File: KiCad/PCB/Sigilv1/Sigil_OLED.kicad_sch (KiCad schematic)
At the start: 3 parts, among them J2 INLAND 1.3" OLED HEADER (7-PI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, J3 BUZZER LOGICAL ONLY, U1 REMOVABLE ESP32 DEVKIT / 2 x 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

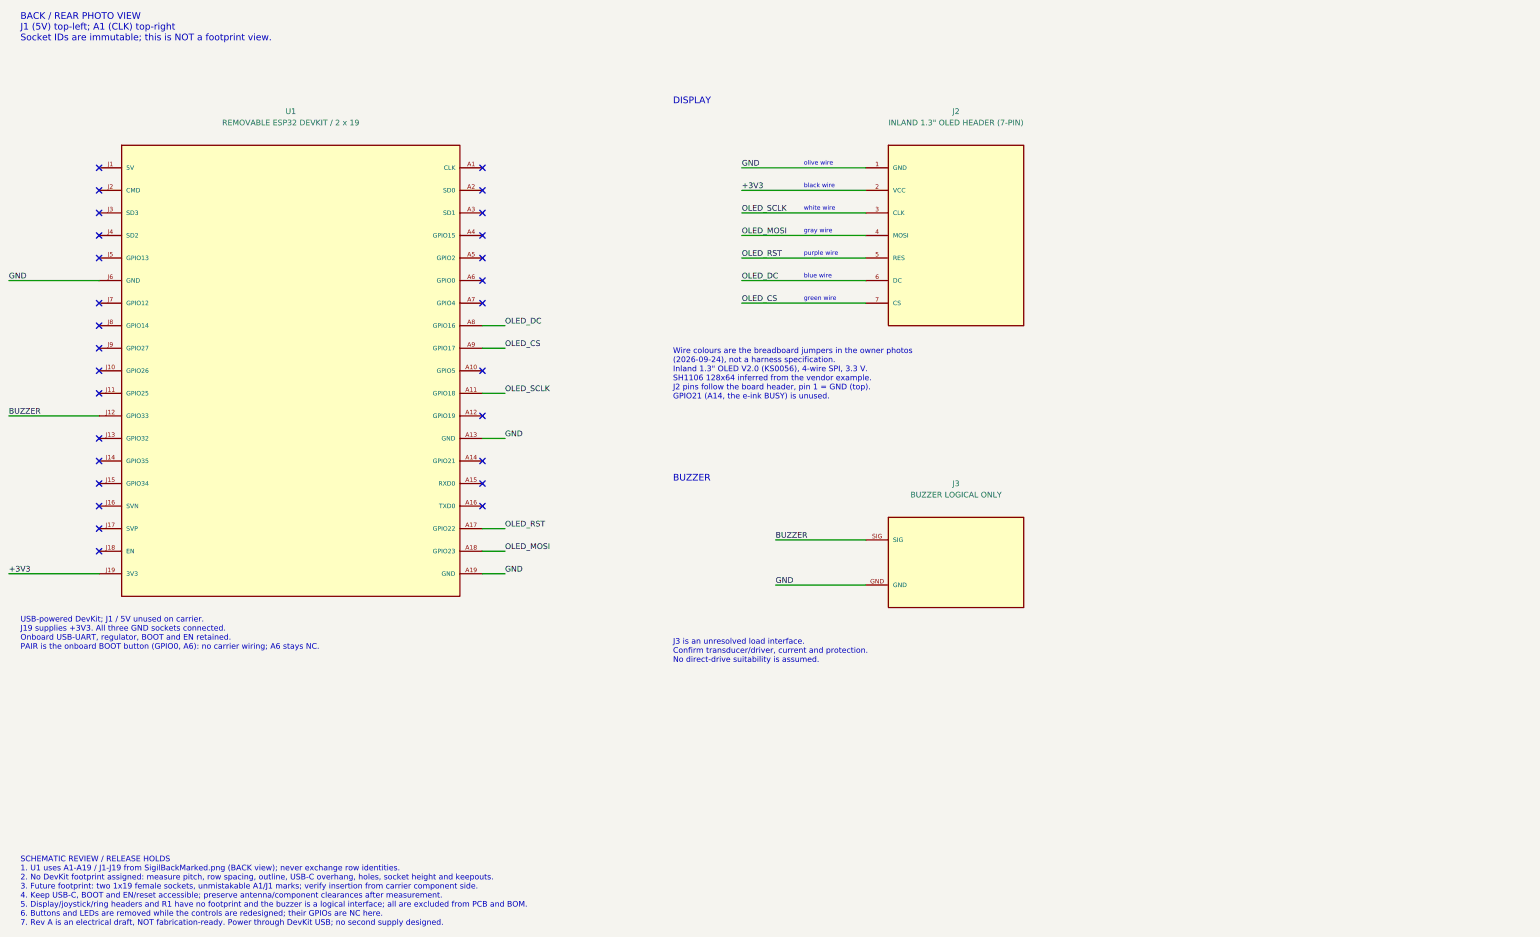
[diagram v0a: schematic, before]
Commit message: New LED Ring
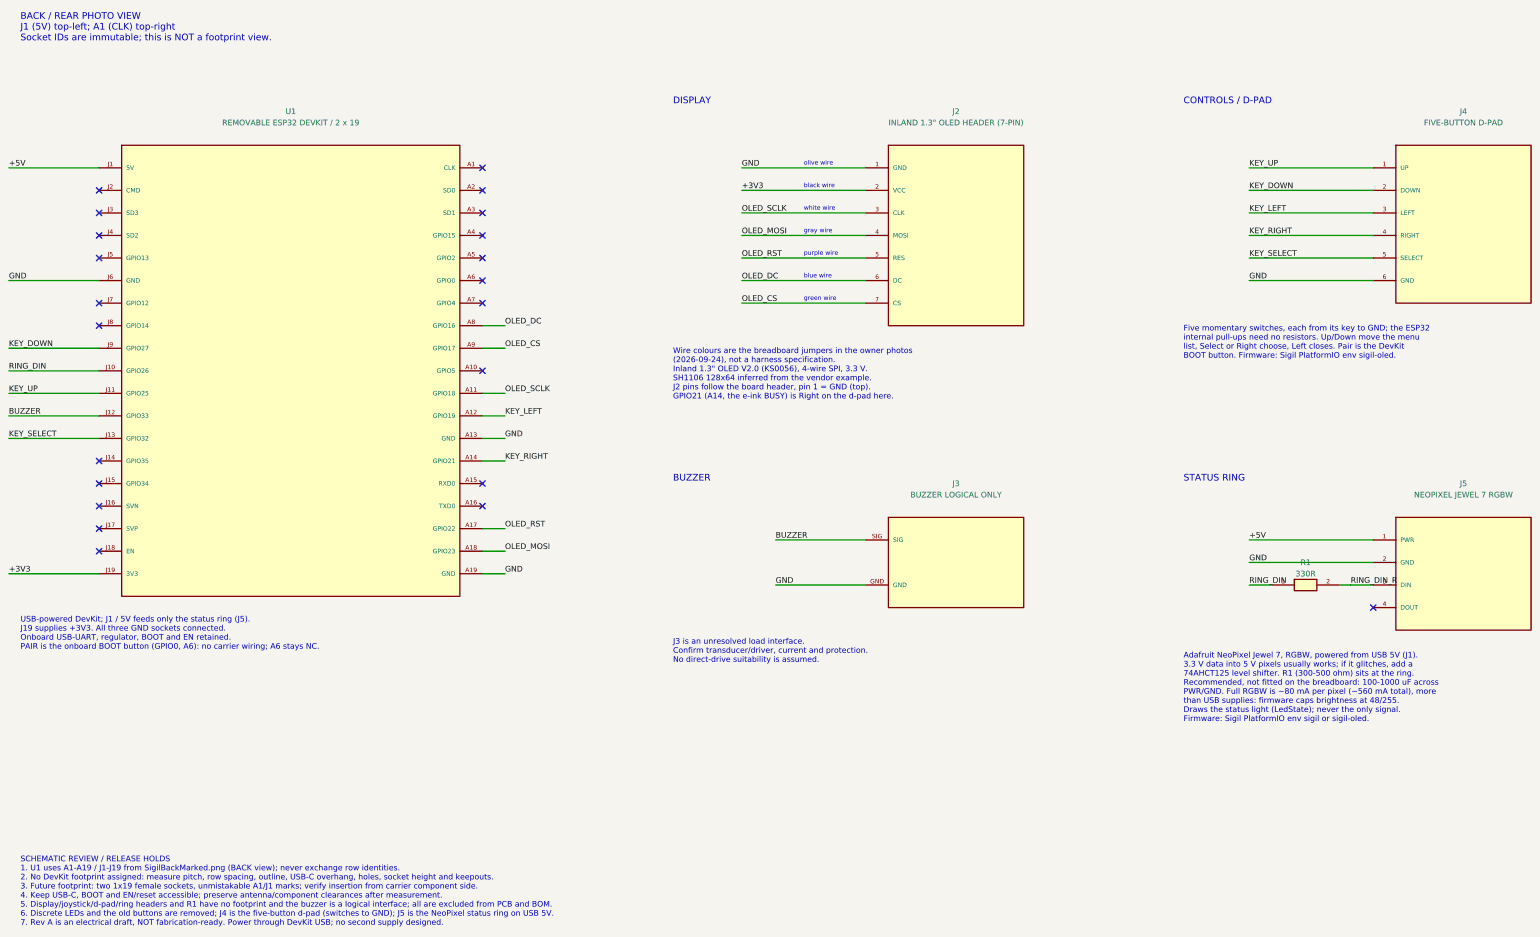
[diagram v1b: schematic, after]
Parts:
- added J4: FIVE-BUTTON D-PAD, symbol Sigil:DPad_5_Key_Header
- added J5: NEOPIXEL JEWEL 7 RGBW, symbol Sigil:NeoPixel_Jewel7_RGBW
- added R1: 330R, symbol Sigil:Resistor_Series
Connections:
- net GND: now also J4.6 (GND), J5.2 (GND)
- net KEY_LEFT: now reaches U1.A12 (GPIO19)
- net KEY_LEFT: now also J4.3 (LEFT)
- net KEY_RIGHT: now reaches U1.A14 (GPIO21)
- net KEY_RIGHT: now also J4.4 (RIGHT)
- net +5V: now reaches U1.J1 (5V)
- net +5V: now also J5.1 (PWR)
- net RING_DIN: now reaches U1.J10 (GPIO26)
- net RING_DIN: now also R1.1
- net KEY_UP: now reaches U1.J11 (GPIO25)
- net KEY_UP: now also J4.1 (UP)
- net KEY_SELECT: now reaches U1.J13 (GPIO32)
- net KEY_SELECT: now also J4.5 (SELECT)
- net KEY_DOWN: now reaches U1.J9 (GPIO27)
- net KEY_DOWN: now also J4.2 (DOWN)
- new net RING_DIN_R: J5.3 (DIN), R1.2
- no-connect marks 28 -> 22
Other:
- note added: "Adafruit NeoPixel Jewel 7, RGBW, powered from USB 5V (J1). 3.3 V data into 5 V pixels usually works; if it glitches, add a 74AHCT125 level shifter. R1 (300-500 ohm) sits at the ring. Recommended, not fitted on the breadboard: 100-1000 uF across PWR/GND. Full RGBW is ~80 mA per pixel (~560 mA total), more than USB supplies: firmware caps brightness at 48/255. Draws the status light (LedState); nev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"
- note added: "CONTROLS / D-PAD"
- note added: "Five momentary switches, each from its key to GND; the ESP32 internal pull-ups need no resistors. Up/Down move the menu list, Select or Right choose, Left closes. Pair is the DevKit BOOT button. Firmware: Sigil PlatformIO env sigil-oled."
- note added: "STATUS RING"
- note added: "USB-powered DevKit; J1 / 5V feeds only the status ring (J5). J19 supplies +3V3. All three GND sockets connected. Onboard USB-UART, regulator, BOOT and EN retained. PAIR is the onboard BOOT button (GPIO0, A6): no carrier wiring; A6 stays NC."
- note added: "Wire colours are the breadboard jumpers in the owner photos (2026-09-24), not a harness specification. Inland 1.3" OLED V2.0 (KS0056), 4-wire SPI, 3.3 V. SH1106 128x64 inferred from the vendor example. J2 pins follow the board header, pin 1 = GND (top). GPIO21 (A14, the e-ink BUSY) is Right on the d-pad here."
- note removed: "USB-powered DevKit; J1 / 5V unused on carrier. J19 supplies +3V3. All three GND sockets connected. Onboard USB-UART, regulator, BOOT and EN retained. PAIR is the onboard BOOT button (GPIO0, A6): no carrier wiring; A6 stays NC."
- note removed: "Wire colours are the breadboard jumpers in the owner photos (2026-09-24), not a harness specification. Inland 1.3" OLED V2.0 (KS0056), 4-wire SPI, 3.3 V. SH1106 128x64 inferred from the vendor example. J2 pins follow the board header, pin 1 = GND (top). GPIO21 (A14, the e-ink BUSY) is unused."
